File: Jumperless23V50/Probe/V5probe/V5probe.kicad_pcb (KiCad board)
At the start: 2 copper layers, 126.4 x 15.2 mm, 49 parts, among them J1 Conn_01x05_Socket, J2 Probe Needle, J7 ProbeJack, P1 M1.6_SMT_Screw_Post 3mm Height, P2 M1.6_SMT_Screw_Post 3mm Height, P3 M1.6_SMT_Screw_Post 3mm Height, P4 M1.6_SMT_Screw_Post 3mm Height, SW1 Disconnect, SW3 Connect, SW4 SW_DPDT_x2, U1 WS2811

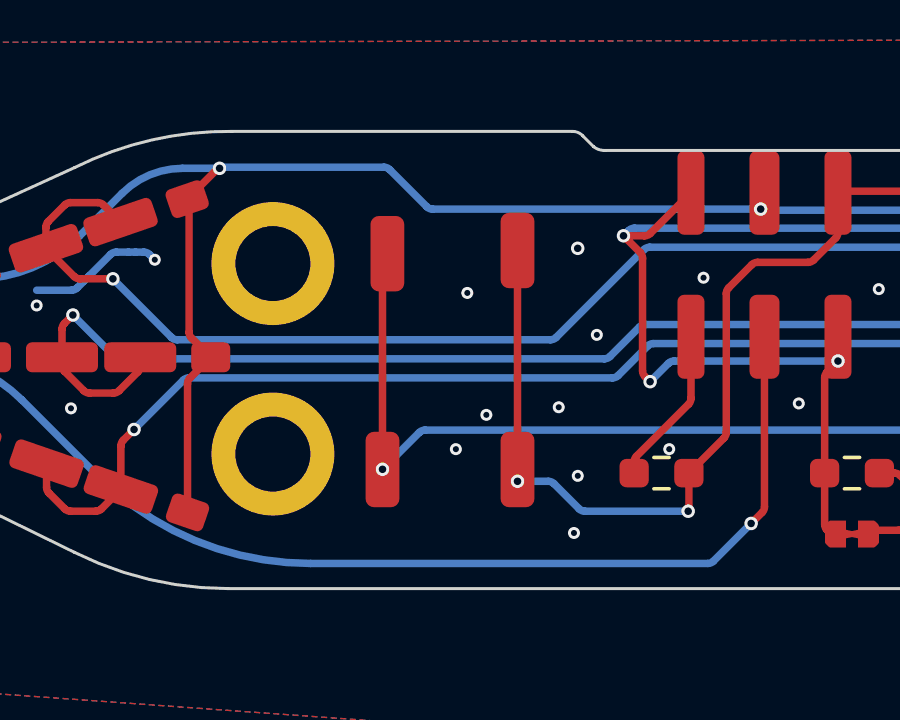
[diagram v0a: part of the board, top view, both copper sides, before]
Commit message: Add related repos as submodules, rev7 hardware update
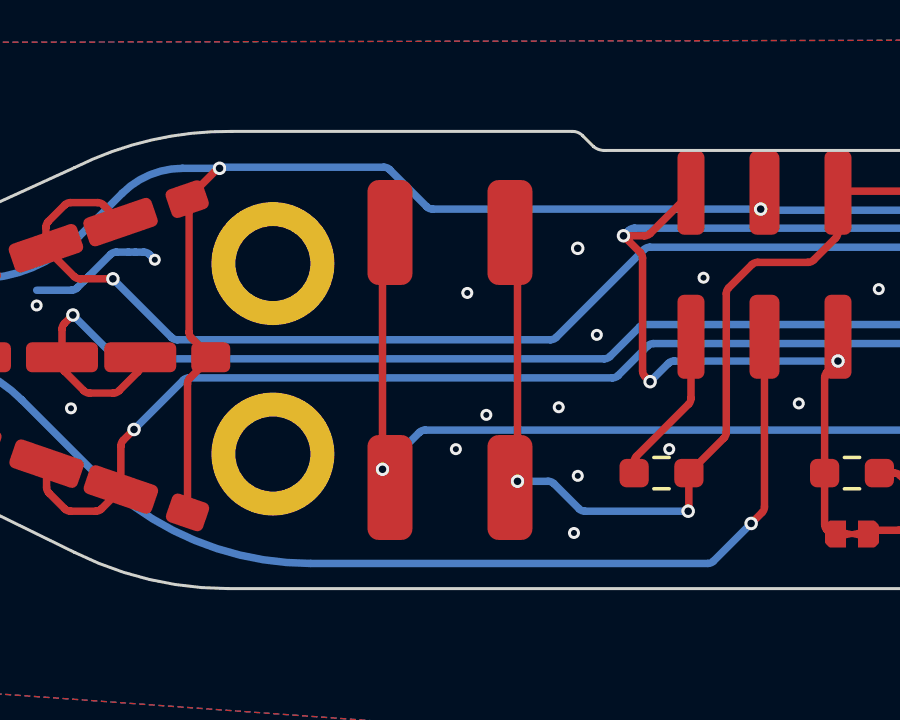
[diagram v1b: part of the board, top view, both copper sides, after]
